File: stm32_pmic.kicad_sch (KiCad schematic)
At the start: 25 parts, among them SW1 EVP-AA602W, SW2 EVP-AA602W, U11 STM32L496RGTx

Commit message: use Common libraries, replace TI MCU with STM32 for CAN bridge
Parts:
- removed D10: ORANGE, LED_SMD:LED_0603_1608Metric, symbol Device:LED
- removed D11: RED, LED_SMD:LED_0603_1608Metric, symbol Device:LED
- removed D12: GREEN, LED_SMD:LED_0603_1608Metric, symbol Device:LED
- removed R36, R37, R38: 680, Resistor_SMD:R_0603_1608Metric_Pad0.98x0.95mm_HandSolder, symbol Device:R
- removed R41: 100K, Resistor_SMD:R_0402_1005Metric_Pad0.72x0.64mm_HandSolder, symbol Device:R
- added C54: 10u, Capacitor_SMD:C_0805_2012Metric_Pad1.18x1.45mm_HandSolder, symbol Device:C
- JP1, JP2: footprint (none) -> Connector_PinHeader_2.54mm:PinHeader_1x02_P2.54mm_Vertical
- SW1, SW2: footprint EVPAA/EVP2A_PAN -> Common:EVP602AA
- renumbered C54 to C55, C55 to C56, C56 to C57, C57 to C58, C58 to C59, C59 to C60, C60 to C61, C61 to C62, C62 to C63, C63 to C64, R35 to R33, R40 to R34, R39 to R35
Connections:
- net 3V3: now also C54.1
- net GND: now also C54.2
- net Schmitt Trigger/IN1: now reaches C64.1, SW1.3
- net Schmitt Trigger/IN1: no longer U11.7 (NRST)
- new net Schmitt Trigger/OUT: U11.7 (NRST)
- no-connect marks 24 -> 27
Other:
- added sheet Schmitt Trigger (../avionics_board/schmitt_trigger.kicad_sch)
- moved on the sheet: C64, JP1, JP2, R34, R35, SW1

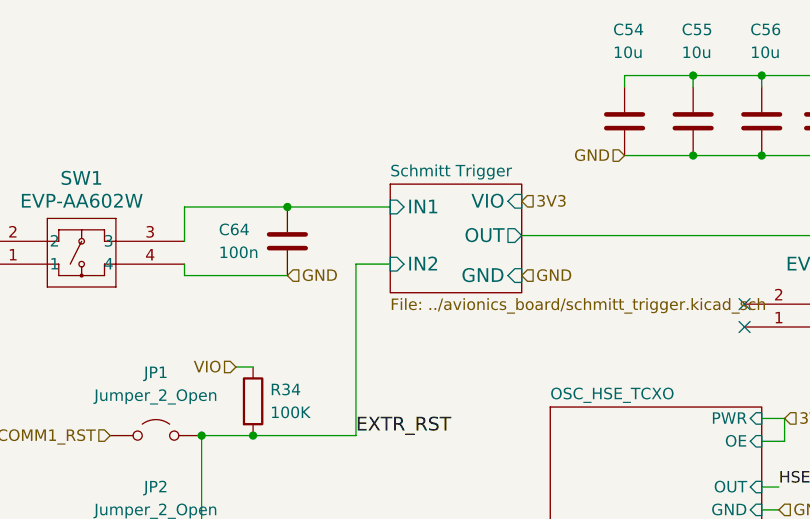
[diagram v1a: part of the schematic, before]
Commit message: openlst board to updated pc104 layout
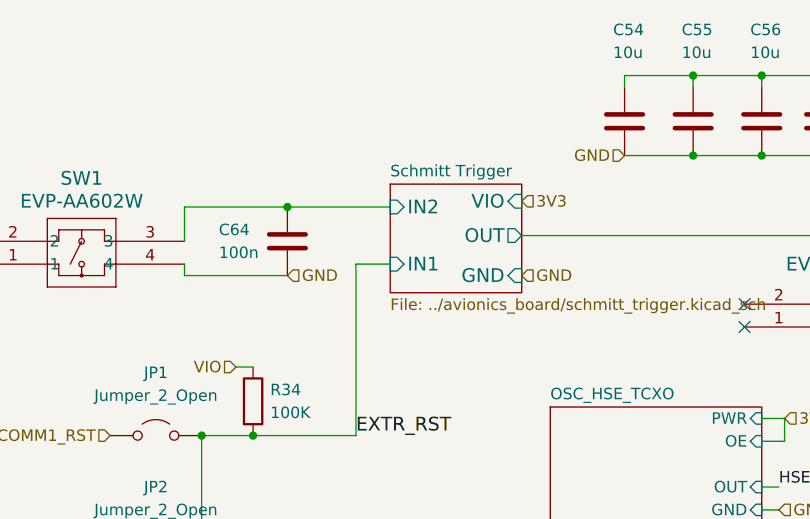
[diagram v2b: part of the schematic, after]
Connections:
- net Schmitt Trigger/IN1 renamed Schmitt Trigger/IN2
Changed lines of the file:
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@@
 	)
 	(junction
+		(at 53.34 49.53)
+		(diameter 0)
+		(color 0 0 0 0)
+	)
+	(junction
 		(at 173.99 141.605)
 		(diameter 0)
@@
 	)
 	(junction
-		(at 53.34 49.53)
-		(diameter 0)
-		(color 0 0 0 0)
-	)
-	(junction
 		(at 171.45 141.605)
 		(diameter 0)
@@
 	(wire
 		(pts
-			(xy 53.34 49.53) (xy 64.77 49.53)
-		)
-		(stroke
-			(width 0)
-			(type default)
-		)
-	)
-	(wire
-		(pts
 			(xy 120.65 43.815) (xy 128.27 43.815)
 		)
@@
 	(wire
 		(pts
+			(xy 60.96 55.88) (xy 64.77 55.88)
+		)
+		(stroke
+			(width 0)
+			(type default)
+		)
+	)
+	(wire
+		(pts
 			(xy 107.95 83.185) (xy 106.045 83.185)
 		)
@@
 	(wire
 		(pts
-			(xy 64.77 55.88) (xy 60.96 55.88)
+			(xy 154.305 85.725) (xy 156.21 85.725)
 		)
 		(stroke
@@
 	(wire
 		(pts
-			(xy 154.305 85.725) (xy 156.21 85.725)
+			(xy 90.805 34.925) (xy 90.805 36.195)
 		)
 		(stroke
@@
 	(wire
 		(pts
-			(xy 90.805 34.925) (xy 90.805 36.195)
+			(xy 128.27 34.925) (xy 128.27 36.195)
 		)
 		(stroke
@@
 	(wire
 		(pts
-			(xy 128.27 34.925) (xy 128.27 36.195)
+			(xy 41.91 49.53) (xy 53.34 49.53)
 		)
 		(stroke
@@
 	(wire
 		(pts
-			(xy 41.91 49.53) (xy 53.34 49.53)
+			(xy 166.37 141.605) (xy 168.91 141.605)
 		)
 		(stroke
@@
 	(wire
 		(pts
-			(xy 166.37 141.605) (xy 168.91 141.605)
+			(xy 143.51 43.815) (xy 151.13 43.815)
 		)
 		(stroke
@@
 	(wire
 		(pts
-			(xy 143.51 43.815) (xy 151.13 43.815)
+			(xy 53.34 49.53) (xy 64.77 49.53)
 		)
 		(stroke
@@
 			)
 		)
-		(pin "IN1" input
+		(pin "IN2" input
 			(at 64.77 49.53 180)
 			(effects
@@
 			)
 		)
-		(pin "IN2" input
+		(pin "IN1" input
 			(at 64.77 55.88 180)
 			(effects

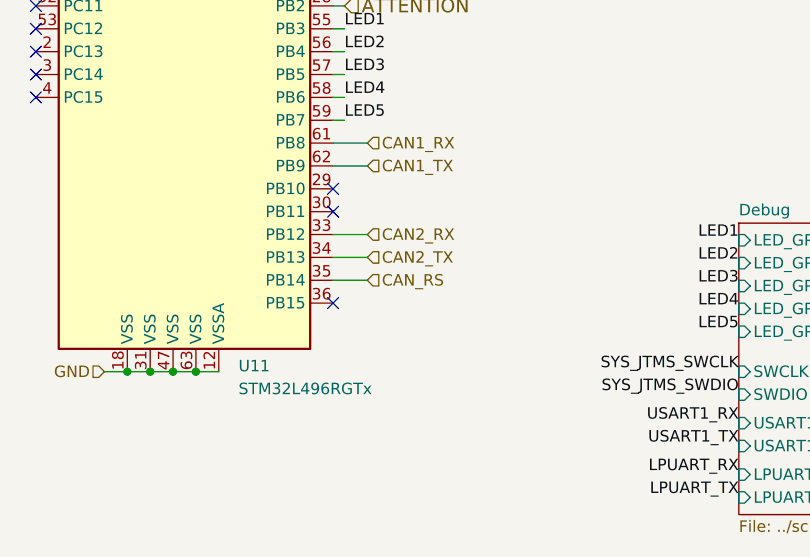
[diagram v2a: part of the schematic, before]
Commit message: replacd TJA1042 with TCAN3414 that allows differential from 3V, negating the need for 5V generator
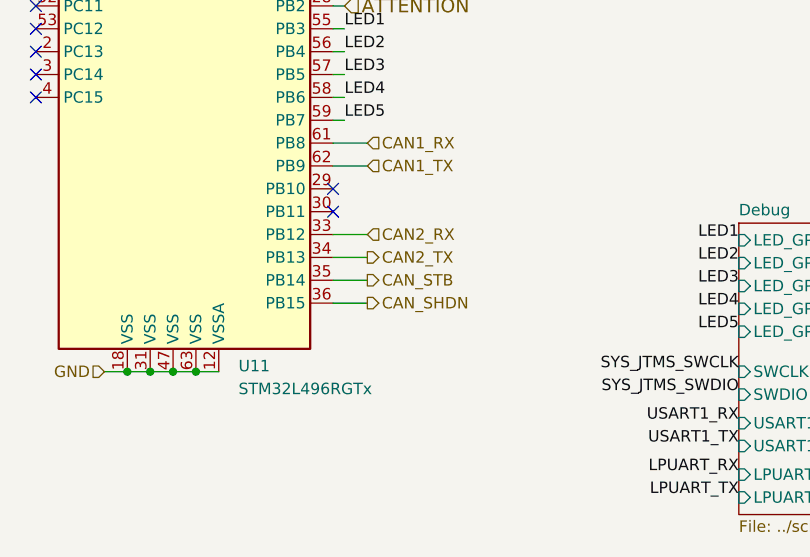
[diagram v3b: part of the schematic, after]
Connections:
- net CAN_SHDN: now reaches U11.36 (PB15)
- net CAN_RS renamed CAN_STB
- no-connect marks 27 -> 26
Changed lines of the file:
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@@
-	)
-	(no_connect
-		(at 189.23 133.985)
 	)
 	(no_connect
@@
 		(pts
 			(xy 43.815 86.995) (xy 43.815 74.93)
+		)
+		(stroke
+			(width 0)
+			(type default)
+		)
+	)
+	(wire
+		(pts
+			(xy 193.04 133.985) (xy 189.23 133.985)
 		)
 		(stroke
@@
 		)
 	)
-	(hierarchical_label "CAN_RS"
-		(shape input)
+	(hierarchical_label "CAN_STB"
+		(shape output)
 		(at 193.04 131.445 0)
 		(fields_autoplaced yes)
@@
 	)
 	(hierarchical_label "CAN2_TX"
-		(shape input)
+		(shape output)
 		(at 193.04 128.905 0)
 		(fields_autoplaced yes)
@@
 		(fields_autoplaced yes)
 		(effects
+			(font
+				(size 1.27 1.27)
+			)
+			(justify left)
+		)
+	)
+	(hierarchical_label "CAN_SHDN"
+		(shape output)
+		(at 193.04 133.985 0)
+		(fields_autoplaced yes)
+		(effects
